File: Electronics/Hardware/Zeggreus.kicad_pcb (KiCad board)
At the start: 4 copper layers, 96.5 x 62.4 mm, 181 parts, among them J1 USB_B_Micro, J10 SMA, J11 P1, J12 P2, J13 USART1, J14 PC5, J2 Batt, J3 Servo1, J4 Servo2, J5 Servo3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

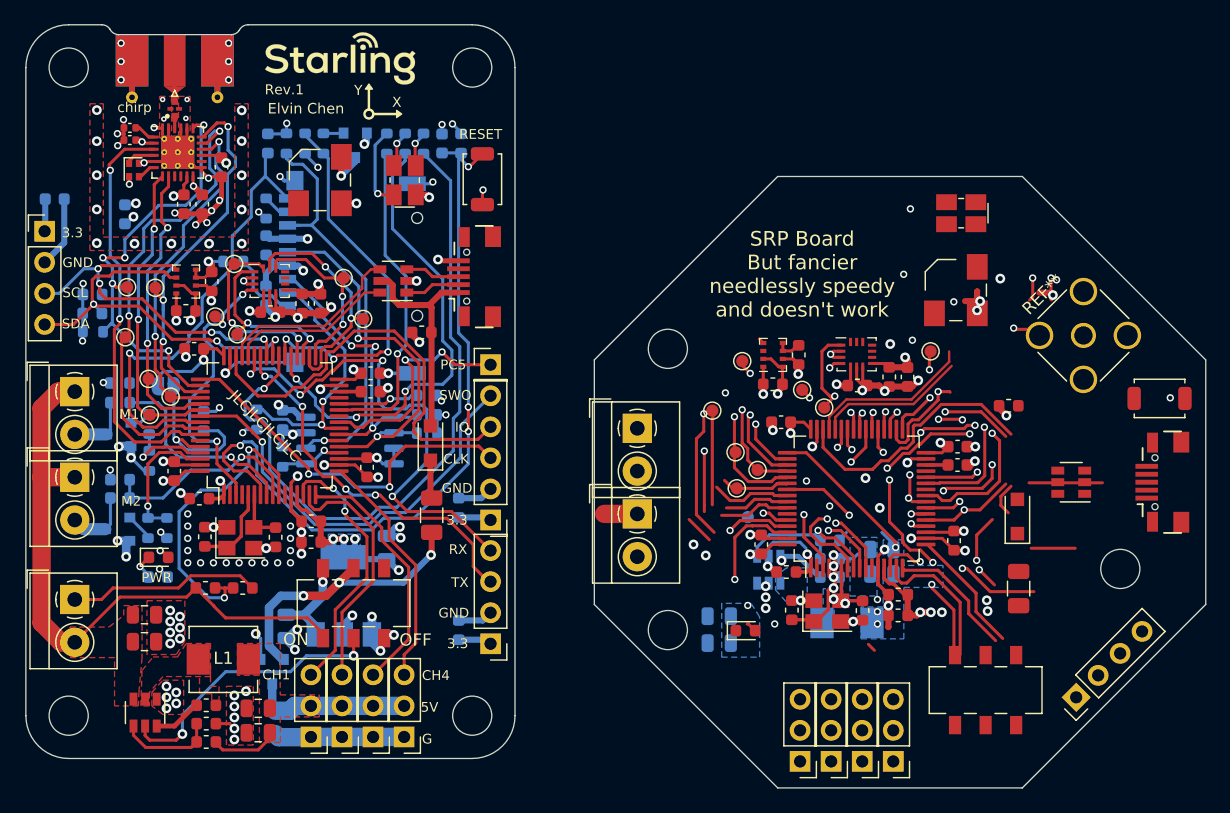
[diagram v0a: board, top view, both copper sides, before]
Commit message: Antenna model and PCB tweaks
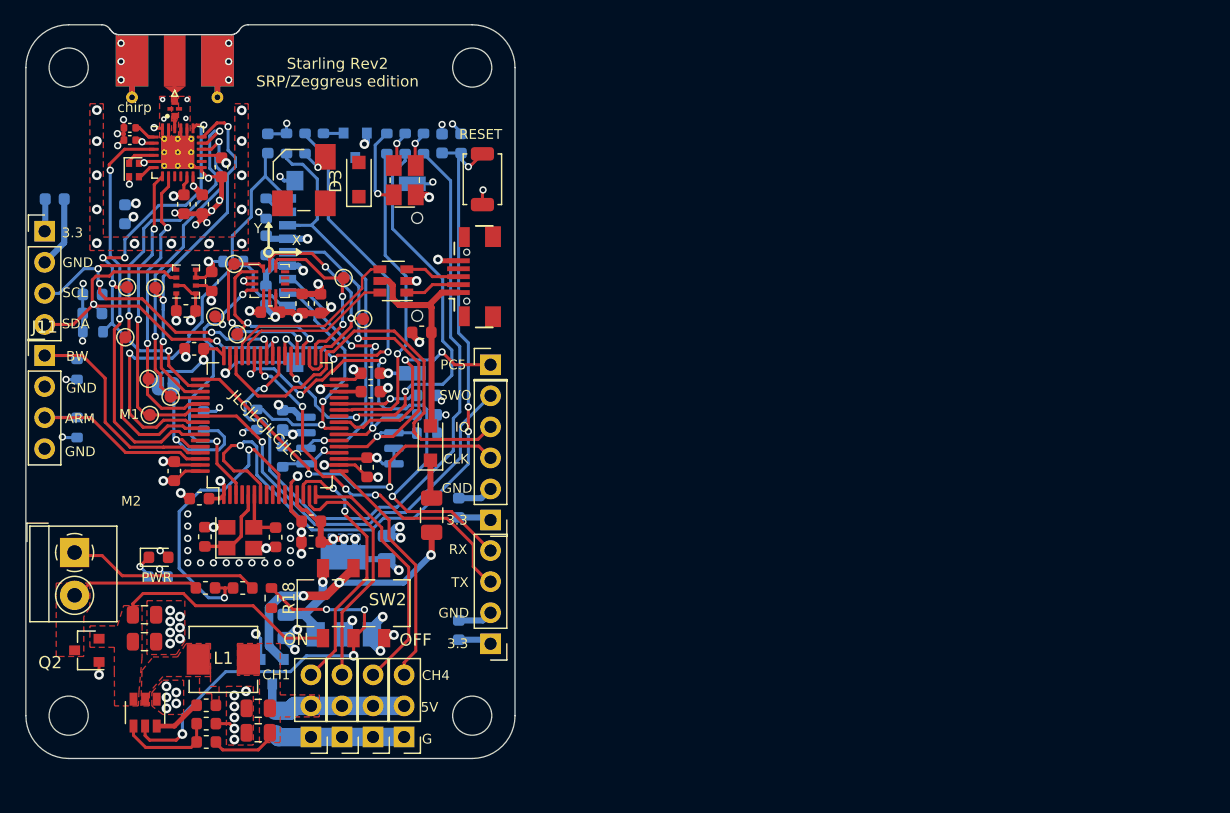
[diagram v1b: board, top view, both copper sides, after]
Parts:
- removed the BZ1 at (204.6, 79.3)
- removed the C1 at (191.7, 84.6)
- removed the C10 at (191.2, 105.5)
- removed the C11 at (190.7, 102.3)
- removed the C12 at (204.7, 93.6)
- removed the C15 at (185.2, 108.2)
- removed the C16 at (188.7, 100.1)
- removed the C17 at (204.7, 92.1)
- removed the C19 at (194.3, 102.8)
- removed the C20 at (208.9, 88.8)
- removed the C23 at (190.3, 90.1)
- removed the C24 at (198.5, 100.5)
- removed the C26 at (185.2, 106.0)
- removed the C27 at (200.6, 86.4)
- removed the C3 at (204.4, 99.8)
- removed the C33 at (198.5, 102.5)
- removed the C4 at (189.6, 87.0)
- removed the C5 at (199.9, 104.2)
- removed the C6 at (199.8, 105.9)
- removed the C7 at (196.9, 105.5)
- removed the C8 at (196.5, 87.1)
- removed the C9 at (199.1, 86.4)
- removed the D1 at (187.4, 107.1)
- removed the D2 at (205.0, 73.0)
- removed the D4 at (209.6, 97.8)
- removed the F1 at (209.7, 103.7)
- removed G***: LOGO, starling:logo
- removed the H1 at (218.0, 102.1)
- removed the H1 at (181.0, 107.1)
- removed the H1 at (181.0, 84.1)
- removed the J1 at (223.0, 95.0)
- removed the J11 at (178.5, 90.6)
- removed the J11 at (132.5, 87.6)
- removed J12 (x2): P2, starling:TerminalBlock_4Ucon_1x02_P3.50mm_Horizontal_blue
- removed the J13 at (214.4, 112.6)
- removed the J3 at (191.8, 117.8)
- removed the J4 at (194.4, 117.8)
- removed the J5 at (196.9, 117.8)
- removed the J6 at (199.4, 117.8)
- removed the L1 at (195.7, 106.5)
- removed Q3: DMN2041L, Package_TO_SOT_SMD:SOT-23
- removed the R12 at (194.3, 99.8)
- removed the R13 at (194.3, 101.3)
- removed R16: 47k, Resistor_SMD:R_0603_1608Metric
- removed R17: 10k, Resistor_SMD:R_0603_1608Metric
- removed R19, R32: 100R, Resistor_SMD:R_0603_1608Metric
- removed R24: 1k, Resistor_SMD:R_0603_1608Metric
- removed REF**: SMA_Amphenol_132291-12_Vertical, Connector_Coaxial:SMA_Amphenol_132291-12_Vertical
- removed the SW1 at (221.2, 88.2)
- removed SW3 (x2): SW_DPDT_x2, starling:SW_DPDT_MST22D18G2
- removed the TP1 at (187.6, 97.8)
- removed the TP11 at (186.7, 95.5)
- removed the TP2 at (202.5, 84.3)
- removed the TP3 at (192.0, 87.5)
- removed the TP5 at (193.8, 88.9)
- removed the TP6 at (188.3, 94.0)
- removed the TP7 at (187.1, 85.1)
- removed the TP8 at (186.6, 92.5)
- removed the TP9 at (184.7, 89.2)
- removed the U1 at (189.6, 84.6)
- removed the U2 at (196.5, 84.5)
- removed the U6 at (189.3, 102.2)
- removed the U7 at (196.5, 96.3)
- removed the U8 at (214.0, 95.0)
- removed the Y1 at (194.1, 105.5)
- added D3: Schottky, Diode_SMD:D_SOD-123F, F.Cu at (155.8, 70.2)
- added J11: Switches, Connector_PinHeader_2.54mm:PinHeader_1x04_P2.54mm_Vertical, F.Cu at (130.1, 84.6)
- added SW2: SW_DPDT_x2, starling:SW_DPDT_MST22D18G2, F.Cu at (155.3, 104.9)
- Q2: value DMN2041L -> AO3401A; moved to F.Cu
- R14: value 47k -> 10k
- R18: value 1k -> 10k; moved to F.Cu
- moved Q2 17.9 mm to (133.5, 108.8)
- moved R18 15.0 mm to (148.6, 104.5)
- moved R15 5.05 mm to (132.7, 90.5), turned to 270 degrees
- moved R14 4.44 mm to (132.7, 85.8), turned to 270 degrees
- moved J2 3.84 mm to (132.5, 100.8)
- moved BZ1 1.32 mm to (151.2, 70.3)
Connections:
- C15 pad 1: +BATT -> bat
- C26 pad 2: +BATT -> bat
- C29 pad 1: +3V3 -> Net-(C29-Pad1)
- Q2 pad 1: Net-(Q2-Pad1) -> Earth
- Q2 pad 2: Earth -> bat
- Q2 pad 3: Net-(J11-Pad2) -> +BATT
- R14 pad 1: M1ADC -> BREAKWIRE
- R14 pad 2: Net-(J11-Pad2) -> +3V3
- R15 pad 1: Earth -> ARM
- R15 pad 2: M1ADC -> +3V3
- R18 pad 1: M1 -> 5V_EN
- R18 pad 2: Earth -> bat
- U6 pad 3: +BATT -> bat
- U7 pad 61: M1 -> BREAKWIRE
- U7 pad 62: M2 -> ARM
- U7 pad 8: M1ADC -> Net-(U7-Pad8)
- U7 pad 9: M2ADC -> Net-(U7-Pad9)
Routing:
- net (no net): track 492.3 -> 0.00 mm, vias 126 -> 0
- net +BATT: track 51.0 -> 11.7 mm
- net BREAKWIRE: track 0.00 -> 20.9 mm
- net bat: track 0.00 -> 18.3 mm
- net M1ADC: track 18.1 -> 0.00 mm, vias 1 -> 0
- net ARM: track 0.00 -> 16.8 mm
- net M2ADC: track 16.7 -> 0.00 mm, vias 1 -> 0
- net 5V_EN: track 23.2 -> 34.2 mm, vias 2 -> 4
- net M2: track 10.9 -> 0.00 mm, vias 1 -> 0
- net Earth: track 183.0 -> 174.8 mm, vias 119 -> 113
- net M1: track 7.32 -> 0.00 mm, vias 1 -> 0
- net Net-(J12-Pad2): track 5.53 -> 0.00 mm
- net Net-(J11-Pad2): track 5.33 -> 0.00 mm
- net Net-(BZ1-Pad2): track 3.54 -> 0.00 mm, vias 1 -> 0
- net Net-(Q3-Pad1): track 2.30 -> 0.00 mm
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- added copper zone on F.Cu, net bat
- removed copper zone on B.Cu, net (none)
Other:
- board size 96.5 x 62.4 mm -> 40 x 60 mm
- board text added: "ARM"
- board text added: "BW"
- board text added: "Starling Rev2 SRP/Zeggreus edition"
- board text removed: "Elvin Chen"
- board text removed: "Rev.1"
- board text removed: "SRP Board But fancier needlessly speedy and doesn't work"

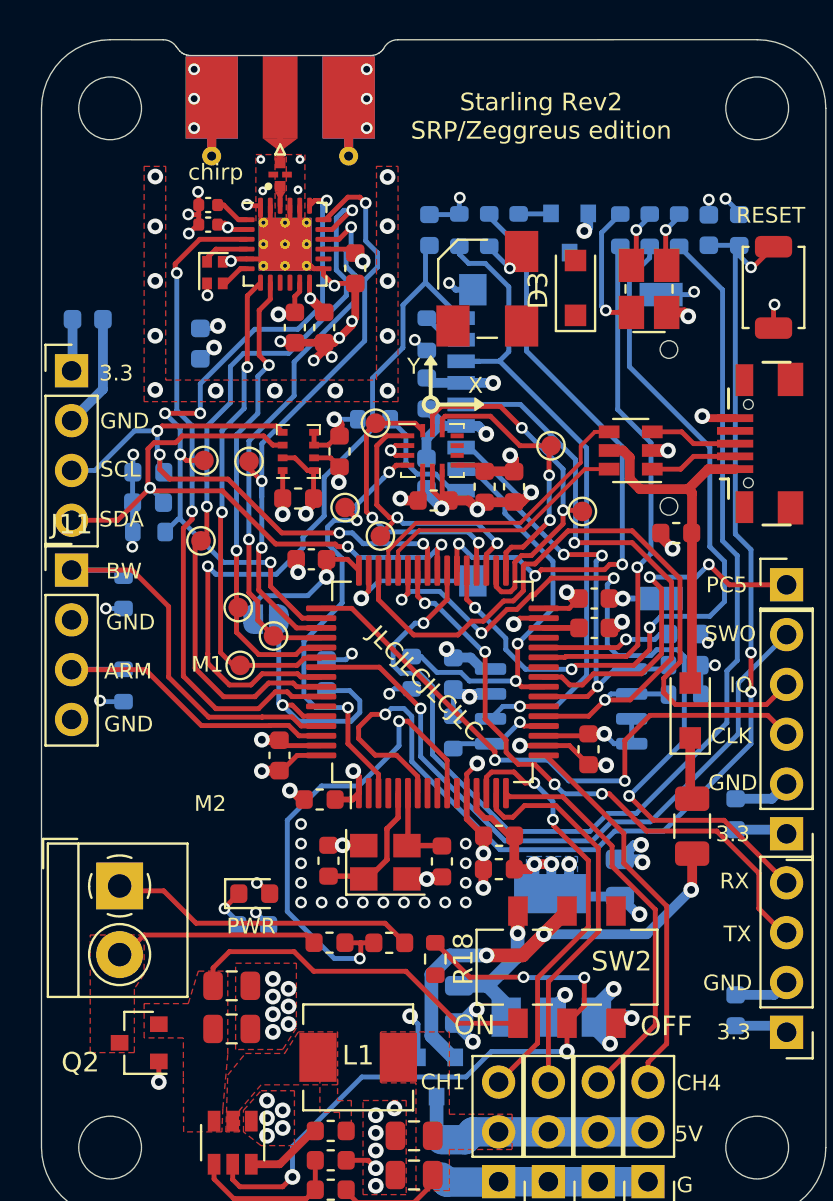
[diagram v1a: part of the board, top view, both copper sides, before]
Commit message: update electronics and added camera model
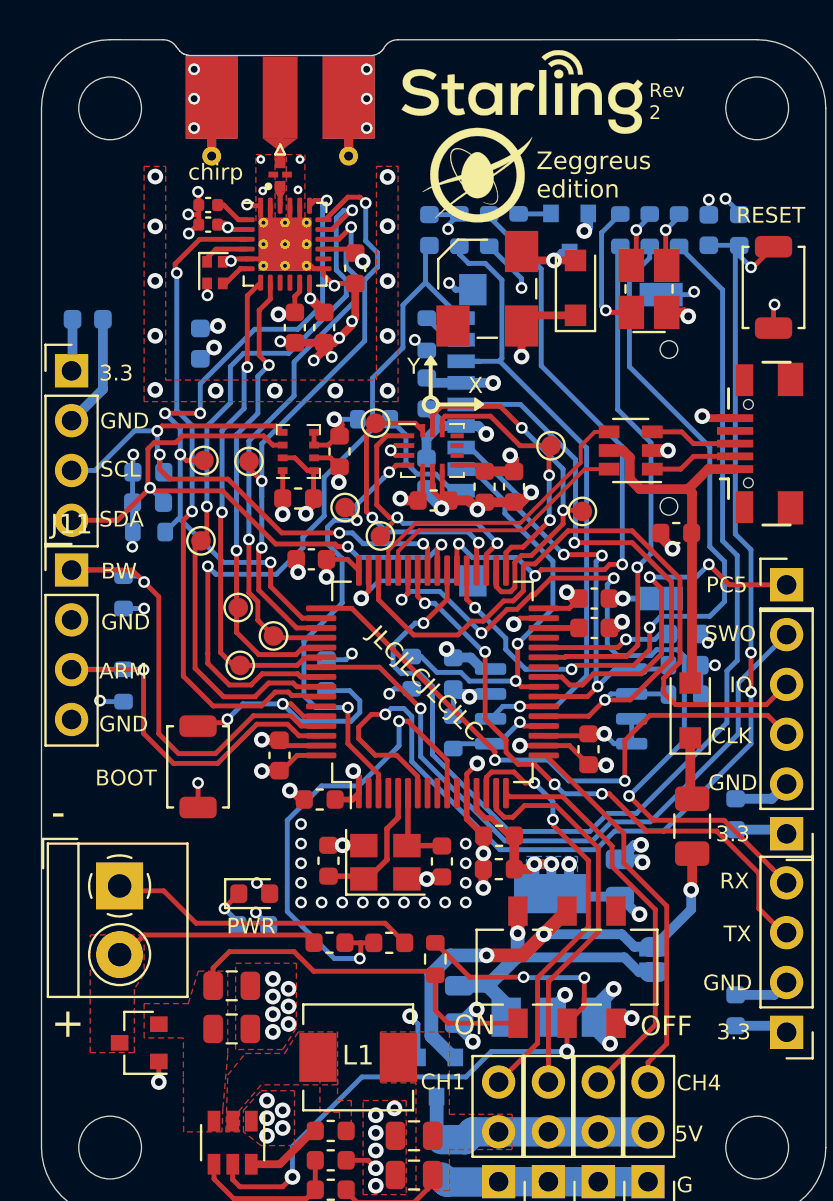
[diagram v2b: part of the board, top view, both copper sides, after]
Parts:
- added G***: LOGO, starling:zeggreus, F.Cu at (150.8, 64.5)
- added G***: LOGO, starling:logo, F.Cu at (153.0, 60.2)
- added SW3: boot, starling:SW_Push_SPST_3×4×2, F.Cu at (136.5, 94.7)
- JP1: value BOOT1 -> SW_bypass
- moved JP1 26.3 mm to (159.8, 104.5), turned to 270 degrees
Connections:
- C29 pad 1: Net-(C29-Pad1) -> +3V3
- JP1 pad 1: BOOT0 -> Net-(F1-Pad1)
- JP1 pad 2: +3V3 -> Net-(C14-Pad2)
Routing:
- net Net-(C14-Pad2): track 7.90 -> 15.2 mm
- net BREAKWIRE: track 20.9 -> 25.7 mm, vias 0 -> 1
- net ARM: track 16.8 -> 21.4 mm, vias 0 -> 1
- net Net-(BZ1-Pad2): track 0.00 -> 3.91 mm, vias 0 -> 1
- net Earth: track 174.8 -> 176.0 mm
- net Net-(F1-Pad1): track 23.4 -> 24.5 mm
- net bat: track 18.3 -> 19.4 mm
- net +3V3: track 97.2 -> 98.1 mm, vias 30 -> 32
- net BOOT0: track 13.7 -> 13.9 mm, vias 1 -> 2
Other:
- board text added: "BOOT"
- board text added: "Rev 2"
- board text added: "Zeggreus edition"
- board text removed: "BOOT0"
- board text removed: "M1"
- board text removed: "M2"
- board text removed: "Starling Rev2 SRP/Zeggreus edition"
